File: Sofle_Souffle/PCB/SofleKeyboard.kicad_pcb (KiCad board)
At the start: 2 copper layers, 84 parts, among them J2 4PIN, J3 OLED, P1 i2c_pin, P2 i2c_pin, SW1 SW_PUSH-MX_W_LED, SW10 SW_PUSH-MX_W_LED, SW11 SW_PUSH-MX_W_LED, SW12 SW_PUSH-MX_W_LED, SW13 SW_PUSH-MX_W_LED, SW14 SW_PUSH-MX_W_LED, SW15 SW_PUSH-MX_W_LED, SW16 SW_PUSH-MX_W_LED, SW17 SW_PUSH-MX_W_LED, SW18 SW_PUSH-MX_W_LED, SW19 SW_PUSH-MX_W_LED, SW2 SW_PUSH-MX_W_LED, SW20 SW_PUSH-MX_W_LED, SW21 SW_PUSH-MX_W_LED, SW22 SW_PUSH-MX_W_LED, SW23 SW_PUSH-MX_W_LED, SW24 SW_PUSH-MX_W_LED, SW25 Rotary_Encoder_Switch, SW26 SW_PUSH-MX_W_LED, SW27 SW_PUSH-MX_W_LED, SW28 SW_PUSH-MX_W_LED, SW29 SW_PUSH-MX_W_LED, SW3 SW_PUSH-MX_W_LED, SW30 SW_PUSH-MX_W_LED, SW4 SW_PUSH-MX_W_LED, SW5 SW_PUSH-MX_W_LED, SW6 SW_PUSH-MX_W_LED, SW7 SW_PUSH-MX_W_LED, SW8 SW_PUSH-MX_W_LED, SW9 SW_PUSH-MX_W_LED, U1 ProMicro

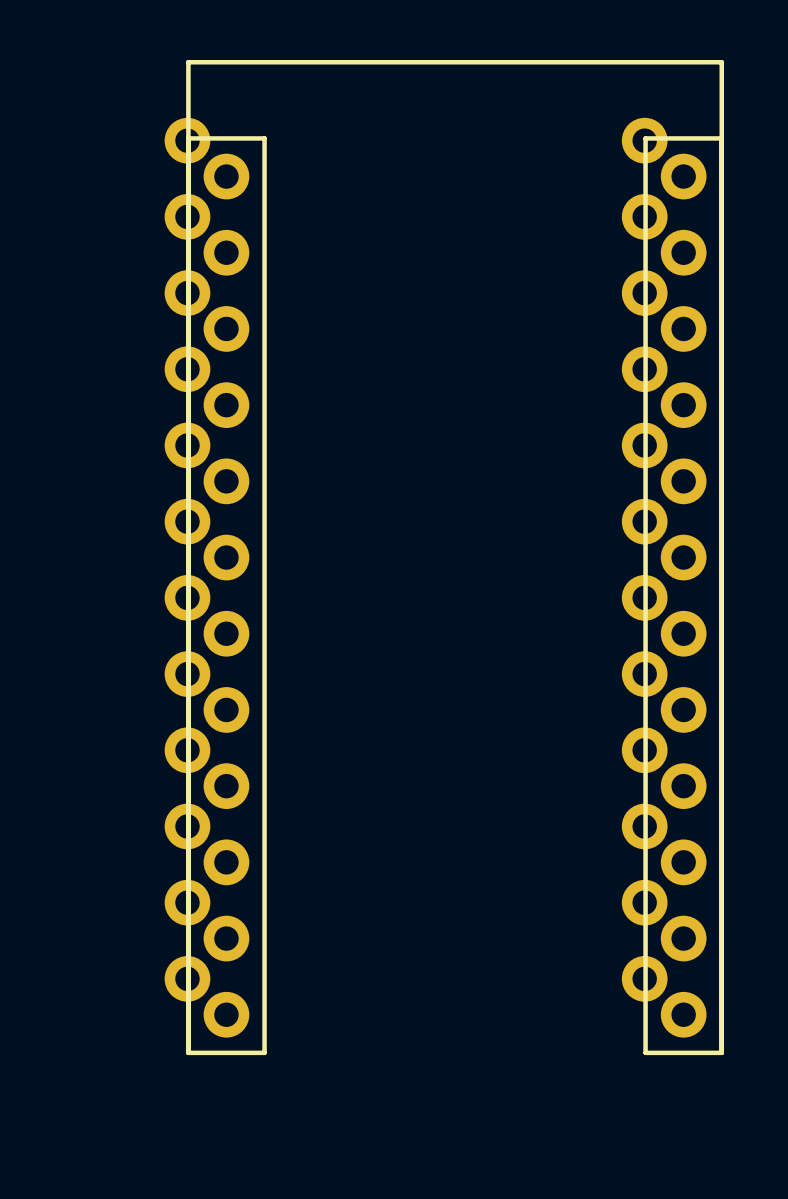
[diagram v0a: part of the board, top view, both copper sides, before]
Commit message: New track added.
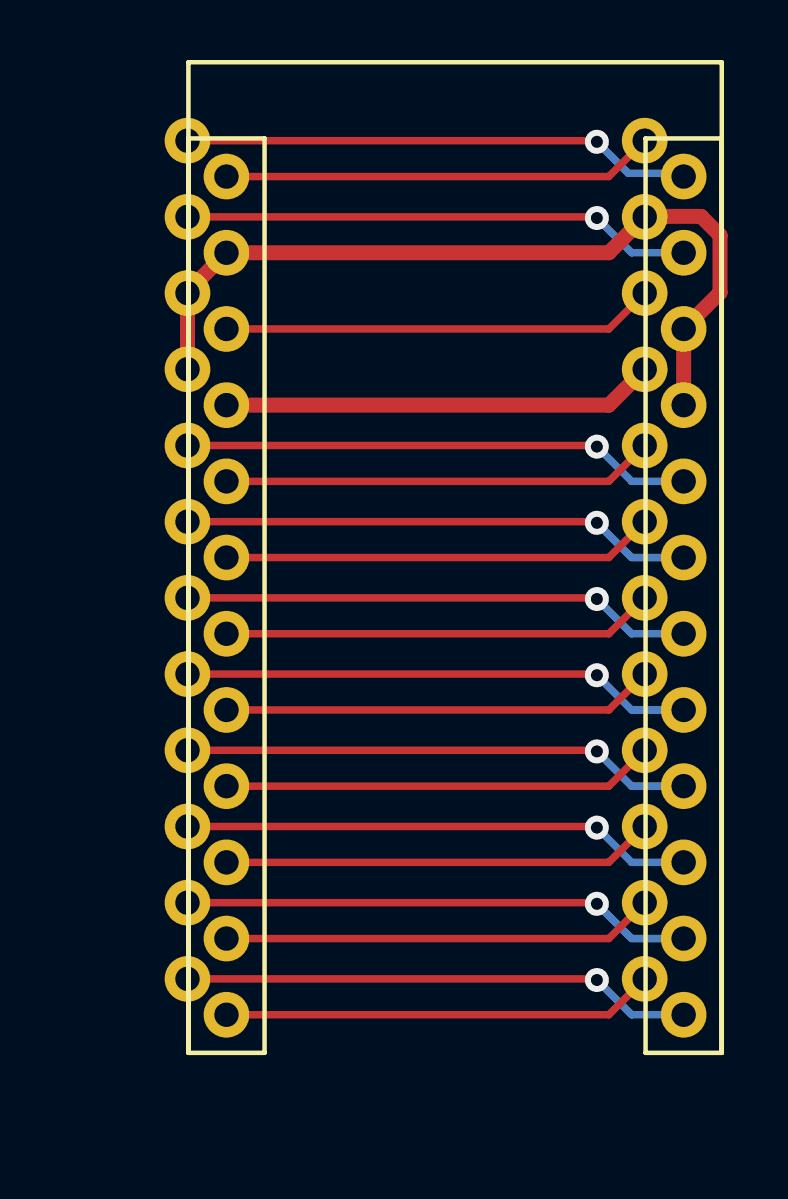
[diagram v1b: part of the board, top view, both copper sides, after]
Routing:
- net GND: track 0.00 -> 27.8 mm
- net row4: track 0.00 -> 17.0 mm, vias 0 -> 1
- net row2: track 0.00 -> 17.0 mm, vias 0 -> 1
- net row0: track 0.00 -> 17.0 mm, vias 0 -> 1
- net SDA: track 0.00 -> 17.0 mm, vias 0 -> 1
- net SCL: track 0.00 -> 17.0 mm, vias 0 -> 1
- net Net-(U1-Pad7): track 0.00 -> 17.0 mm, vias 0 -> 1
- net row3: track 0.00 -> 17.0 mm, vias 0 -> 1
- net row1: track 0.00 -> 17.0 mm, vias 0 -> 1
- net LED: track 0.00 -> 17.0 mm, vias 0 -> 1
- net DATA: track 0.00 -> 17.0 mm, vias 0 -> 1
- net col4: track 0.00 -> 14.4 mm
- net col3: track 0.00 -> 14.4 mm
- net col2: track 0.00 -> 14.4 mm
- net col1: track 0.00 -> 14.4 mm
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
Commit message: Completed Soufflé board with palm key. Missing the roller encoder.
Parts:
- added ?: , , F.Cu at (102.6, 82.8)
- added ?: , , F.Cu at (102.6, 80.0)
- added GND1: col_pin, SofleRGB:1pin_conn, F.Cu at (102.6, 80.0)
- added LED1: col_pin, SofleRGB:1pin_conn, F.Cu at (102.6, 82.8)
- added TH8: HOLE, SofleRGB:M2_HOLE_PCB, F.Cu at (95.8, 94.7)
- added VCC1: col_pin, SofleRGB:1pin_conn, F.Cu at (102.6, 85.6)
- D30: footprint SofleRGB:Jumper -> SofleRGB:crkbd-diode
- J2: footprint SofleRGB:Jumper -> SofleRGB:MJ-4PP-9
- J3: footprint SofleRGB:Jumper -> SofleRGB:OLED_4Pin
- JP5, JP6, JP7, JP8: moved to B.Cu
- SW1, SW10, SW11, SW12, SW13, SW14, SW15, SW16, SW17, SW18, SW19, SW2, SW20, SW21, SW22, SW23, SW24, SW26, SW27, SW28, SW29, SW3, SW30, SW4, SW5, SW6, SW7, SW8, SW9: footprint SofleRGB:SK6812MINI_and_cherry -> SofleRGB:SK6812MINI_and_cherry_NoLEDPads
- moved SW18 379.4 mm to (209.0, 92.7), turned to 180 degrees
- moved SW30 377.5 mm to (209.0, 130.8), turned to 180 degrees
- moved D12 369.5 mm to (200.7, 71.9), turned to 270 degrees
- moved D11 360.2 mm to (198.4, 71.9), turned to 270 degrees
- moved D18 357.1 mm to (200.7, 90.9), turned to 270 degrees
- moved SW23 356.6 mm to (190.0, 111.7), turned to 180 degrees
- moved SW24 355.0 mm to (209.0, 111.7), turned to 180 degrees
- moved D6 354.1 mm to (200.7, 52.8), turned to 270 degrees
- moved D5 351.1 mm to (198.4, 52.8), turned to 270 degrees
- moved D17 343.4 mm to (198.4, 90.9), turned to 270 degrees
- moved SW15 340.5 mm to (151.9, 85.3), turned to 180 degrees
- moved SW29 338.9 mm to (151.9, 123.4), turned to 180 degrees
- moved D10 334.6 mm to (162.6, 64.3), turned to 270 degrees
- moved D24 333.7 mm to (200.7, 110.0), turned to 270 degrees
- moved TH5 331.4 mm to (199.3, 63.8), turned to 180 degrees
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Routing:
- net col0: track 14.4 -> 289.8 mm, vias 0 -> 5
- net col1: track 14.4 -> 288.4 mm, vias 0 -> 6
- net col2: track 14.4 -> 248.8 mm, vias 0 -> 5
- net col4: track 14.4 -> 241.4 mm, vias 0 -> 5
- net col3: track 14.4 -> 235.6 mm, vias 0 -> 5
- net row4: track 17.0 -> 163.8 mm, vias 1 -> 7
- net SW25A: track 14.4 -> 153.1 mm, vias 0 -> 4
- net row3: track 17.0 -> 146.1 mm, vias 1 -> 7
- net row0: track 17.0 -> 130.1 mm, vias 1 -> 7
- net row2: track 17.0 -> 129.6 mm, vias 1 -> 7
- net row1: track 17.0 -> 120.0 mm, vias 1 -> 7
- net GND: track 27.8 -> 114.2 mm, vias 0 -> 16
- net ENCB: track 14.4 -> 74.7 mm, vias 0 -> 1
- net Net-(D26-Pad2): track 0.00 -> 58.5 mm, vias 0 -> 2
- net ENCA: track 14.4 -> 72.1 mm, vias 0 -> 1
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- added copper zone on B.Cu, net GND
- added copper zone on F.Cu, net GND
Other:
- board outline added: 143.3 x 111.7 mm
- net class Default: via_dia 0.8 -> 0.4; via_drill 0.4 -> 0.3
- net class GND added: clearance 0.2, trace_width 0.5, via_dia 0.4, via_drill 0.3
- net class VCC added: clearance 0.2, trace_width 0.5, via_dia 0.4, via_drill 0.3

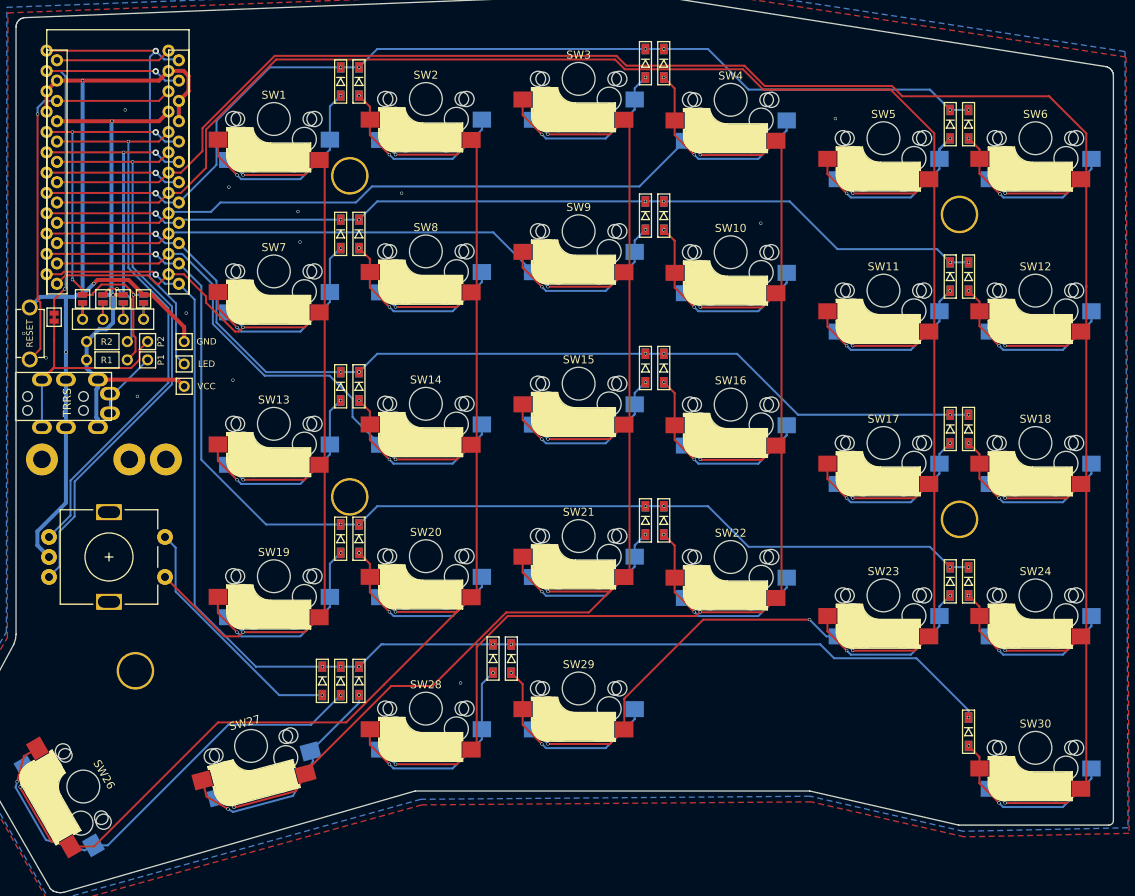
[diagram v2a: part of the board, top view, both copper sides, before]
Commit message: Added EVQWGD001 and 5pin to schematic, and 5pin to PCB.
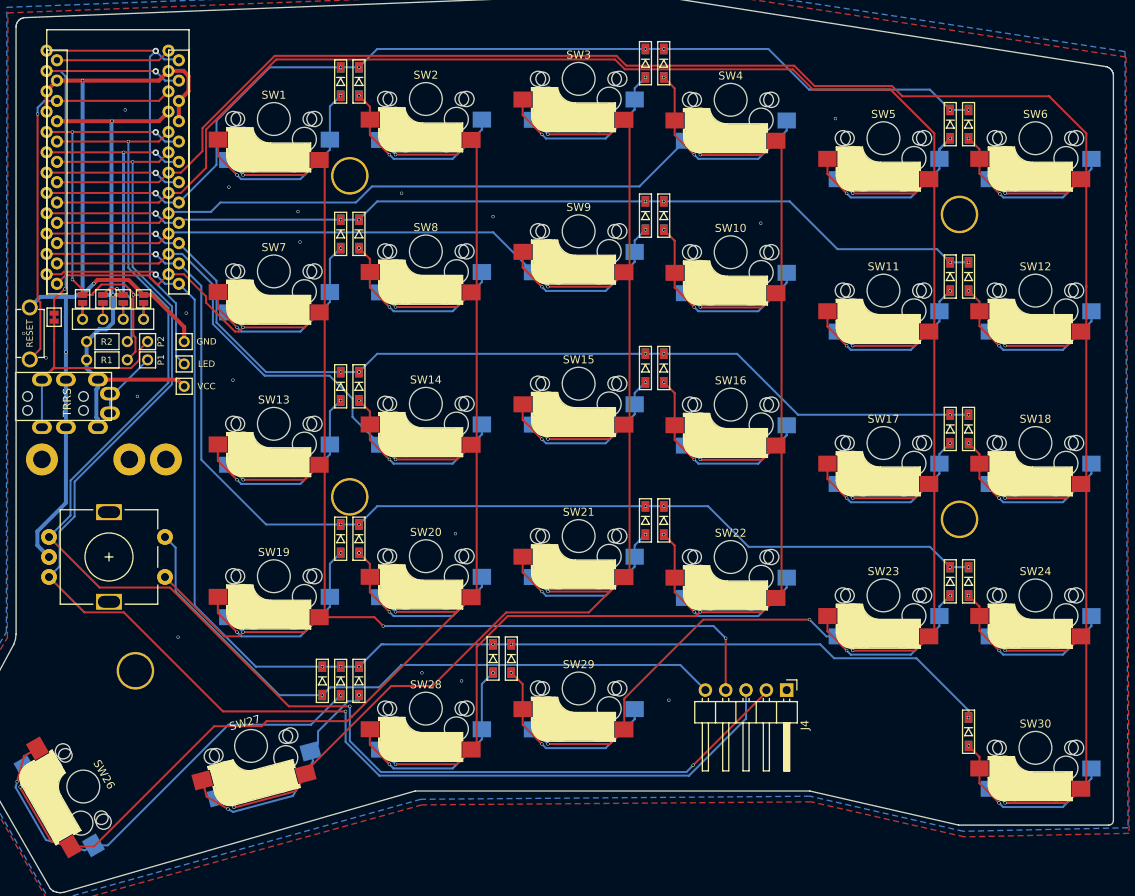
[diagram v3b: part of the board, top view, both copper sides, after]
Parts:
- removed the ? at (102.6, 82.8)
- removed the ? at (102.6, 80.0)
- added ?: , , F.Cu at (102.4, 84.1)
- added ?: , , F.Cu at (102.4, 81.3)
- added J4: Conn_01x05_Female, Connector_PinHeader_2.54mm:PinHeader_1x05_P2.54mm_Horizontal, F.Cu at (177.9, 123.6)
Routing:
- net ENCA: track 72.1 -> 180.9 mm, vias 1 -> 3
- net ENCB: track 74.7 -> 180.9 mm, vias 1 -> 2
- net SW25A: track 153.1 -> 211.5 mm, vias 4 -> 6
- net SW25B: track 31.1 -> 81.8 mm
- net Net-(D27-Pad2): track 29.5 -> 30.3 mm
- net GND: vias 16 -> 21
